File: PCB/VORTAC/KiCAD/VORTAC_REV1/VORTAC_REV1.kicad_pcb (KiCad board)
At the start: 4 copper layers, 68.4 x 24.7 mm, 13 parts, among them IC1 TMC2209-LA, J14 918-418K2023S40001, J15 STEPPER, J16 IO, J2 Molex Micro Fit 3.0, U2 STM32F103C8Tx, U6 SN65HVD232DR

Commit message: hallo
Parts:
- removed D7: NeoPixel_THT, LED_SMD:LED_Cree-PLCC4_2x2mm_CW
- removed J16: IO, Connector_JST:JST_PH_B5B-PH-K_1x05_P2.00mm_Vertical
- removed J2: Molex Micro Fit 3.0, Connector_JST:JST_PH_B6B-PH-K_1x06_P2.00mm_Vertical
- added C11: 0.1uF 50V, Capacitor_SMD:C_0603_1608Metric, F.Cu at (99.2, 69.1)
- added C12: 3.3nF, Capacitor_SMD:C_0603_1608Metric, F.Cu at (99.2, 71.6)
- added C14: 56pF, Capacitor_SMD:C_0603_1608Metric, F.Cu at (99.2, 74.2)
- added C16: 47uF, Capacitor_SMD:C_0805_2012Metric, F.Cu at (103.4, 76.8)
- added C18: 47uF, Capacitor_SMD:C_0805_2012Metric, F.Cu at (103.4, 79.9)
- added C20: 47uF, Capacitor_SMD:C_0805_2012Metric, F.Cu at (103.4, 82.9)
- added C21: 0.1uF 50V, Capacitor_SMD:C_0603_1608Metric, F.Cu at (127.1, 61.6)
- added C22: 0.1uF 50V, Capacitor_SMD:C_0603_1608Metric, F.Cu at (127.1, 64.1)
- added C23: 22nF X7R 10% 50V, Capacitor_SMD:C_0603_1608Metric, F.Cu at (127.1, 66.6)
- added C24: 0.1uF 50V, Capacitor_SMD:C_0603_1608Metric, F.Cu at (127.1, 69.1)
- added C26: 0.1uF 50V, Capacitor_SMD:C_0603_1608Metric, F.Cu at (127.1, 71.6)
- added C29: 0.1uF 50V, Capacitor_SMD:C_0603_1608Metric, F.Cu at (127.1, 74.2)
- added C3: 1uF, Capacitor_SMD:C_0603_1608Metric, F.Cu at (99.2, 61.6)
- added C33: 0.1uF 16V, Capacitor_SMD:C_0402_1005Metric, F.Cu at (120.8, 61.3)
- added C35: 0.1uF 16V, Capacitor_SMD:C_0402_1005Metric, F.Cu at (120.8, 63.3)
- added C36: 0.1uF 16V, Capacitor_SMD:C_0402_1005Metric, F.Cu at (120.8, 65.3)
- added C37: 0.1uF 16V, Capacitor_SMD:C_0402_1005Metric, F.Cu at (120.8, 67.2)
- added C38: 0.1uF 16V, Capacitor_SMD:C_0402_1005Metric, F.Cu at (120.8, 69.2)
- added C39: 0.1uF 16V, Capacitor_SMD:C_0402_1005Metric, F.Cu at (120.8, 71.2)
- added C40: 4.7uF 10V, Capacitor_SMD:C_0402_1005Metric, F.Cu at (123.7, 61.3)
- added C42: C_Small, Capacitor_SMD:C_0402_1005Metric, F.Cu at (123.7, 63.3)
- added C43: C_Small, Capacitor_SMD:C_0402_1005Metric, F.Cu at (123.7, 65.3)
- added C44: 10nF, Capacitor_SMD:C_0402_1005Metric, F.Cu at (123.7, 67.2)
- added C45: 1uF, Capacitor_SMD:C_0402_1005Metric, F.Cu at (123.7, 69.2)
- added C49: 0.1uF 16V, Capacitor_SMD:C_0402_1005Metric, F.Cu at (112.7, 81.0)
- added C5: 10uF 50V, Capacitor_SMD:C_1206_3216Metric, F.Cu at (108.5, 77.0)
- added C7: 0.1uF 50V, Capacitor_SMD:C_0603_1608Metric, F.Cu at (99.2, 64.1)
- added C8: 1uF, Capacitor_SMD:C_0603_1608Metric, F.Cu at (99.2, 66.6)
- added D5: D_Schottky, Diode_SMD:D_SOD-123, F.Cu at (127.0, 85.8)
- added D6: LED_Small, LED_SMD:LED_0402_1005Metric, F.Cu at (130.8, 61.3)
- added J1: DEBUG, ToolChanger:PinHeader_2x03_P1.27mm_Vertical, F.Cu at (146.7, 130.1)
- added J3: Conn_01x05, Connector_PinHeader_2.54mm:PinHeader_1x05_P2.54mm_Vertical, F.Cu at (174.2, 119.4)
- added L3: 10uH 15mA, Inductor_SMD:L_0805_2012Metric, F.Cu at (121.7, 73.5)
- added R1: 1K, Resistor_SMD:R_0603_1608Metric, F.Cu at (115.7, 88.5)
- added R2: 2K, Resistor_SMD:R_0603_1608Metric, F.Cu at (115.7, 90.5)
- added R23: 10k, Resistor_SMD:R_0402_1005Metric, F.Cu at (110.5, 88.0)
- added R25: 95k, Resistor_SMD:R_0402_1005Metric, F.Cu at (110.5, 90.0)
- added R28: 100k, Resistor_SMD:R_0402_1005Metric, F.Cu at (110.5, 92.0)
- added R29: 19.1k, Resistor_SMD:R_0402_1005Metric, F.Cu at (110.5, 94.0)
- added R3: 5.12K, Resistor_SMD:R_0402_1005Metric, F.Cu at (125.5, 88.5)
- added R31: 1K, Resistor_SMD:R_0402_1005Metric, F.Cu at (130.6, 63.3)
- added R32: 22K, Resistor_SMD:R_0402_1005Metric, F.Cu at (130.6, 65.3)
- added R33: 22K, Resistor_SMD:R_0402_1005Metric, F.Cu at (130.6, 67.3)
- added R35: 22R, Resistor_SMD:R_0402_1005Metric, F.Cu at (130.6, 69.3)
- added R36: 22R, Resistor_SMD:R_0402_1005Metric, F.Cu at (130.6, 71.3)
- added R37: R_Small, Resistor_SMD:R_0402_1005Metric, F.Cu at (130.6, 73.3)
- added R38: R_Small, Resistor_SMD:R_0402_1005Metric, F.Cu at (130.6, 75.3)
- added R4: 5.12K, Resistor_SMD:R_0402_1005Metric, F.Cu at (125.5, 90.5)
- added R5: 180, Resistor_SMD:R_0603_1608Metric, F.Cu at (115.7, 93.0)
- added R51: 1K, Resistor_SMD:R_0402_1005Metric, F.Cu at (110.5, 96.0)
- added R52: 10K, Resistor_SMD:R_0402_1005Metric, F.Cu at (110.5, 98.0)
- added R6: 180, Resistor_SMD:R_0603_1608Metric, F.Cu at (115.7, 95.5)
- added R7: 1K, Resistor_SMD:R_0603_1608Metric, F.Cu at (115.7, 98.0)
- added R8: 2K, Resistor_SMD:R_0603_1608Metric, F.Cu at (115.7, 100.5)
- added S1: ~, ToolChanger:OPB666N, F.Cu at (150.0, 119.0)
- added S2: ~, ToolChanger:OPB666N, F.Cu at (173.1, 108.5)
- added U1: TLV73333PDBV, Package_TO_SOT_SMD:SOT-23-5, F.Cu at (113.8, 77.7)
- added U3: STM32L011D_3-4_Px, Package_SO:TSSOP-14_4.4x5mm_P0.65mm, F.Cu at (164.0, 101.5)
- added U4: TPS54335ADRCR, ToolChanger:VSON-10-1EP_3x3mm_P0.5mm_EP1.65x2.4mm_ThermalVias, B.Cu at (157.5, 106.5)
- added U5: STM32G0B1C_B-C-E_Tx, Package_QFP:LQFP-48_7x7mm_P0.5mm, B.Cu at (174.5, 79.5)
- IC1: footprint ToolChanger:tmc_2209_ThermalPad -> ToolChanger:tmc_2209_package; moved to F.Cu
- J14: footprint ToolChanger:USB_C_Receptacle_XKB_U262-16XN-4BVC11 -> Connector_USB:USB_C_Receptacle_GCT_USB4115-03-C
- J15: footprint ToolChanger:JST_PH_S4B-PH-K_1x04_P2.00mm_Horizontal -> Connector_JST:JST_PH_B4B-PH-K_1x04_P2.00mm_Vertical; moved to B.Cu
- U6: moved to B.Cu
- moved J14 48.1 mm to (186.3, 101.6), turned to 135 degrees
- moved J15 33.2 mm to (160.5, 120.0), turned to 0 degrees
- moved IC1 23.8 mm to (150.0, 111.5), turned to -90 degrees
- moved C34 12.6 mm to (166.0, 112.5), turned to 0 degrees
- moved HSE1 11.8 mm to (172.9, 115.7)
- moved U2 11.1 mm to (165.8, 109.8)
- moved L2 8.56 mm to (157.0, 111.5)
- moved R30 5.26 mm to (126.5, 118.0), turned to 180 degrees
- moved U6 2.48 mm to (164.0, 101.6), turned to 180 degrees
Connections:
- U2 pad 10: HOST_USB_GATE -> unconnected-(U2-PA0-Pad10)
- U2 pad 11: LED_1_GATE -> unconnected-(U2-PA1-Pad11)
- U2 pad 13: ADXL_INT1 -> unconnected-(U2-PA3-Pad13)
- U2 pad 14: ADXL_CS -> unconnected-(U2-PA4-Pad14)
- U2 pad 15: ADXL_SCL -> unconnected-(U2-PA5-Pad15)
- U2 pad 16: ADXL_SDO -> unconnected-(U2-PA6-Pad16)
- U2 pad 17: ADXL_SDI -> unconnected-(U2-PA7-Pad17)
- U2 pad 21: THERM_1_PIN -> unconnected-(U2-PB10-Pad21)
- U2 pad 22: IO_3_OUT_PIN -> unconnected-(U2-PB11-Pad22)
- U2 pad 25: IO_2_OUT_PIN -> unconnected-(U2-PB12-Pad25)
- U2 pad 26: IO_1_OUT_PIN -> unconnected-(U2-PB13-Pad26)
- U2 pad 27: HEATER_GATE -> unconnected-(U2-PB14-Pad27)
- U2 pad 42: FAN_1_GATE -> unconnected-(U2-PB6-Pad42)
- U2 pad 43: FAN_2_GATE -> unconnected-(U2-PB7-Pad43)

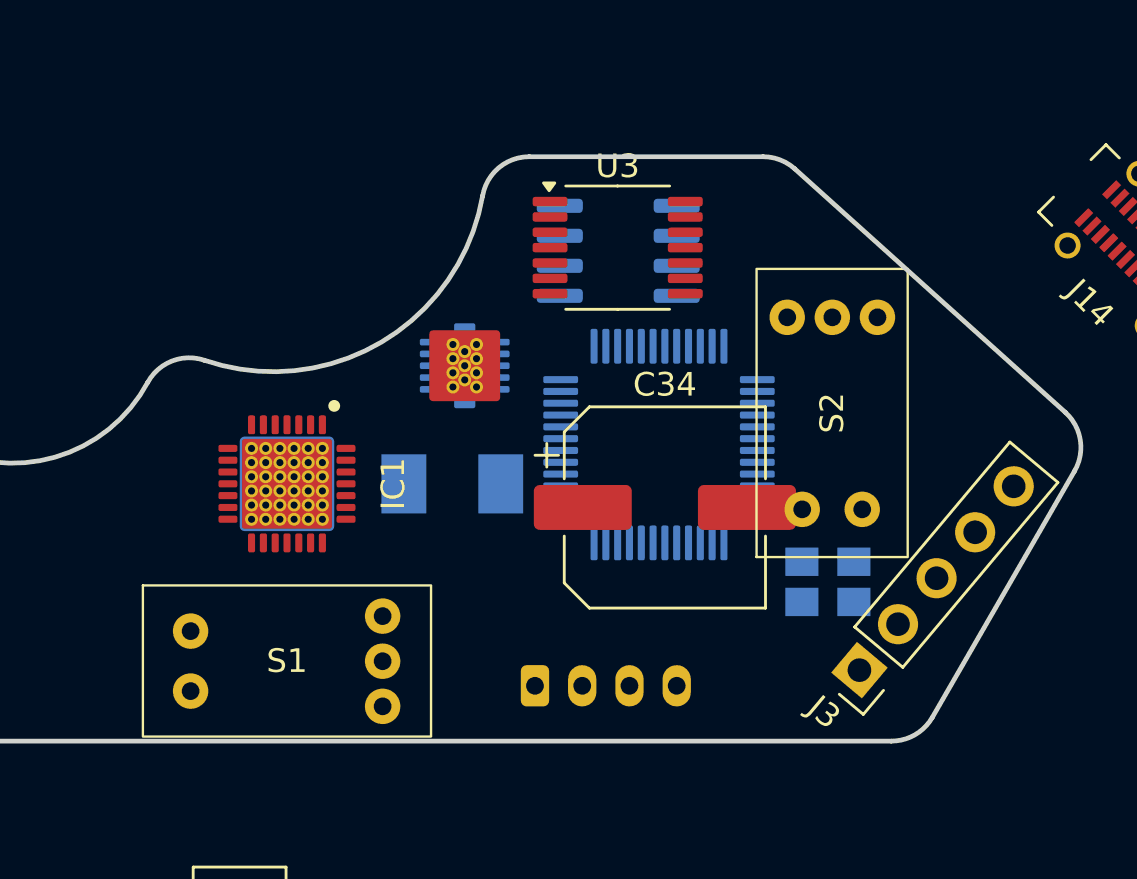
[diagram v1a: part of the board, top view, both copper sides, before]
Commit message: Added New EE_SX3350
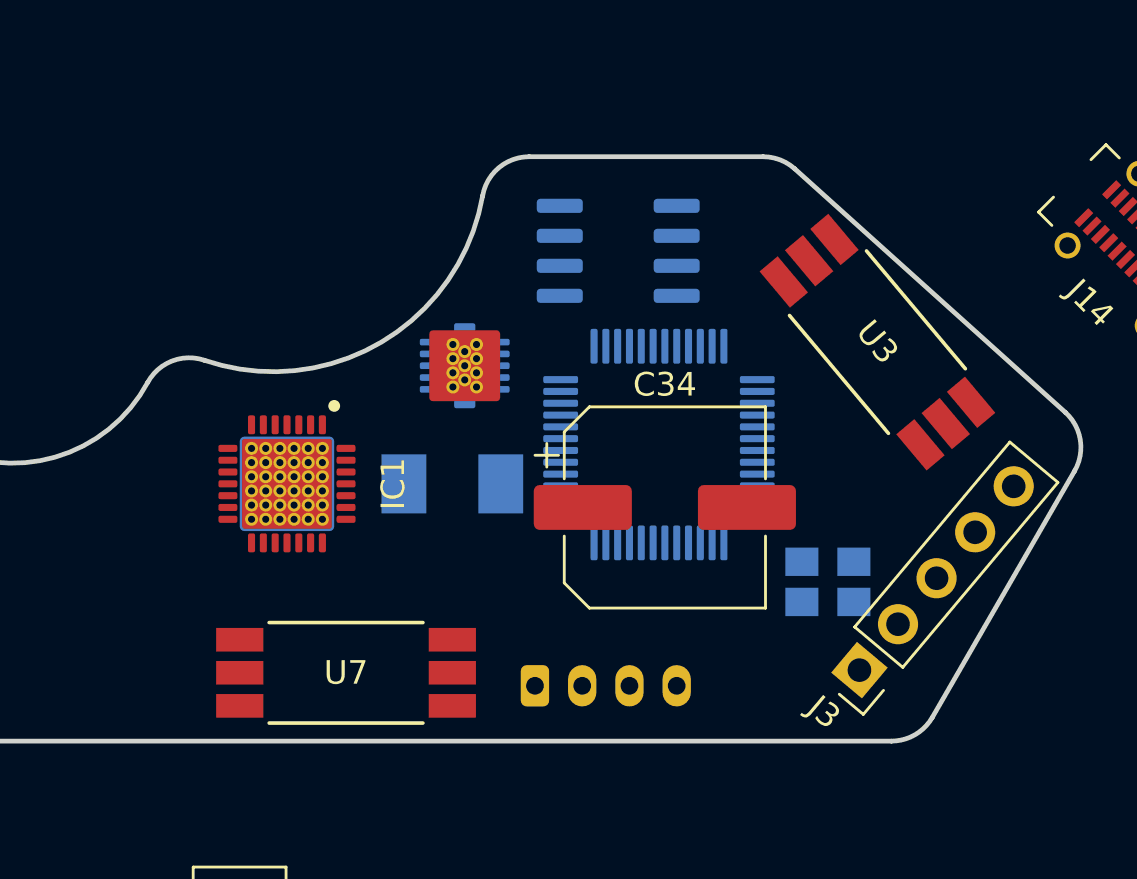
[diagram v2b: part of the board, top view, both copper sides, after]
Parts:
- removed S1, S2: ~, ToolChanger:OPB666N
- added U7: EE-SX3350, ToolChanger:SENSOR_EE-SX3350_OMR, F.Cu at (152.5, 119.5)
- U3: value STM32L011D_3-4_Px -> EE-SX3350; footprint Package_SO:TSSOP-14_4.4x5mm_P0.65mm -> ToolChanger:SENSOR_EE-SX3350_OMR
- moved U3 11.7 mm to (175.0, 105.5), turned to -50 degrees
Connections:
- R1 pad 1: Net-(S1-Out) -> Net-(U3-GND)
- R6 pad 2: Net-(S1-CA) -> Net-(U3-ANODE)
- U3 pad 1: unconnected-(U3-PB9-Pad1) -> Net-(U3-ANODE)
- U3 pad 2: unconnected-(U3-PC14-Pad2) -> GND
- U3 pad 3: unconnected-(U3-PC15-Pad3) -> GND
- U3 pad 4: unconnected-(U3-NRST-Pad4) -> GND
- U3 pad 5: unconnected-(U3-PA0-Pad5) -> +5V
- U3 pad 6: unconnected-(U3-PA1-Pad6) -> Net-(U3-GND)

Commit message: yipppieee
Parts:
- removed R31: 1K, Resistor_SMD:R_0402_1005Metric
- removed U5: STM32G0B1C_B-C-E_Tx, Package_QFP:LQFP-48_7x7mm_P0.5mm
- added C1: 470pF 100V, Capacitor_SMD:C_0603_1608Metric, F.Cu at (139.5, 110.4)
- added C10: 0.1uF 50V, Capacitor_SMD:C_0603_1608Metric, F.Cu at (139.5, 123.0)
- added C2: 0.1uF 50V, Capacitor_SMD:C_0603_1608Metric, F.Cu at (139.5, 112.9)
- added C4: 470pF 100V, Capacitor_SMD:C_0603_1608Metric, F.Cu at (139.5, 115.5)
- added C6: 470pF 100V, Capacitor_SMD:C_0603_1608Metric, F.Cu at (139.5, 118.0)
- added C9: 470pF 100V, Capacitor_SMD:C_0603_1608Metric, F.Cu at (139.5, 120.5)
- added JP1: Jumper, Connector_PinHeader_1.27mm:PinHeader_2x01_P1.27mm_Vertical, F.Cu at (143.7, 110.8)
- added L1: Common Choke, Inductor_SMD:L_CommonModeChoke_Coilcraft_0805USB, F.Cu at (143.0, 114.5)
- added R10: 120R, Resistor_SMD:R_0402_1005Metric, F.Cu at (143.0, 119.5)
- added R9: 100R, Resistor_SMD:R_0402_1005Metric, F.Cu at (143.0, 117.5)
- C22: value 0.1uF 50V -> 4.7uF 50V
- C34: footprint Capacitor_SMD:CP_Elec_8x6.9 -> Capacitor_SMD:CP_Elec_6.3x7.7
- J14: moved to B.Cu
- R30, R34: value 0.1R 1% -> 0.22R 1%
- R32, R33: value 22K -> 10K
- moved J1 33.0 mm to (170.3, 107.0), turned to 180 degrees
- moved U2 21.8 mm to (186.8, 104.2)
- moved J14 13.5 mm to (174.2, 95.3), turned to 0 degrees
- moved J3 10.9 mm to (181.0, 110.8), turned to -30 degrees
- moved U3 3.16 mm to (174.0, 108.5), turned to 90 degrees
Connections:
- IC1 pad 14: TMC_UART_RX -> TMC_UART
- R1 pad 1: Net-(U3-GND) -> Net-(U3-OUTPUT)
- R33 pad 1: TMC_UART_RX -> TMC_UART
- R33 pad 2: GND -> +3V3
- R7 pad 1: Net-(U7-GND) -> Net-(U7-OUTPUT)
- U2 pad 10: unconnected-(U2-PA0-Pad10) -> ENDSTOP_Z
- U2 pad 11: unconnected-(U2-PA1-Pad11) -> ENDSTOP_X
- U2 pad 30: TMC_UART_TX -> TMC_UART
- U2 pad 31: TMC_UART_RX -> unconnected-(U2-PA10-Pad31)
- U2 pad 38: TMC_DIAG -> Net-(U2-PA15)
- U3 pad 4: GND -> +5V
- U3 pad 5: +5V -> Net-(U3-OUTPUT)
- U3 pad 6: Net-(U3-GND) -> GND
- U6 pad 6: CAN_L -> Net-(U6-CANL)
- U6 pad 7: CAN_H -> Net-(U6-CANH)
- U7 pad 4: GND -> +5V
- U7 pad 5: +5V -> Net-(U7-OUTPUT)
- U7 pad 6: Net-(U7-GND) -> GND

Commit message: Fixed Library stuff
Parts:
- added C13: 0.1uF 50V, Capacitor_SMD:C_0603_1608Metric, F.Cu at (173.8, 101.8)
- added R11: 10K, Resistor_SMD:R_0402_1005Metric, F.Cu at (177.7, 110.6)
- added R12: 10K, Resistor_SMD:R_0402_1005Metric, F.Cu at (174.7, 115.4)
- added SW1: Boot, Vortac:KEY-SMD_B3U-1000PM, B.Cu at (162.5, 100.0)
- added SW2: Reset, Vortac:KEY-SMD_B3U-1000PM, B.Cu at (165.8, 100.0)
- C10, C21, C22, C23, C24, C26, C5, C6, C9, D5, JP1, R1, R10, R2, R35, R36, R37, R38, R5, R6, R7, R8, R9: moved to B.Cu
- IC1: footprint ToolChanger:tmc_2209_package -> Vortac:tmc_2209_package
- J1: footprint ToolChanger:PinHeader_2x03_P1.27mm_Vertical -> Vortac:PinHeader_2x03_P1.27mm_Vertical; moved to B.Cu
- J14: footprint Connector_USB:USB_C_Receptacle_GCT_USB4115-03-C -> Vortac:USB-C-TH_HANBO_MC-118LD-H65
- L1: footprint Inductor_SMD:L_CommonModeChoke_Coilcraft_0805USB -> Vortac:L_CommonModeChoke_Coilcraft_0805USB
- L2: footprint ToolChanger:L_Sunlord_MWSA0518_5.4x5.2mm -> Vortac:L_Sunlord_MWSA0518_5.4x5.2mm
- R30, R34, U6: moved to F.Cu
- U2: value STM32F103C8Tx -> STM32F103C8T6
- U3, U7: footprint ToolChanger:SENSOR_EE-SX3350_OMR -> Vortac:SENSOR_EE-SX3350_OMR
- U4: footprint ToolChanger:VSON-10-1EP_3x3mm_P0.5mm_EP1.65x2.4mm_ThermalVias -> Vortac:VSON-10-1EP_3x3mm_P0.5mm_EP1.65x2.4mm_ThermalVias
- moved C11 86.1 mm to (168.8, 119.8)
- moved C12 85.6 mm to (168.8, 121.4)
- moved C18 77.4 mm to (171.8, 116.0)
- moved C20 76.9 mm to (171.8, 118.0)
- moved C14 74.7 mm to (160.0, 117.4)
- moved C3 73.7 mm to (148.6, 116.2)
- moved C7 73.6 mm to (151.6, 115.8)
- moved C5 72.8 mm to (174.5, 107.8), turned to 180 degrees
- moved C8 70.8 mm to (151.6, 114.2)
- moved C21 70.2 mm to (179.6, 108.3), turned to -90 degrees
- moved C40 69.9 mm to (177.7, 105.7)
- moved C22 69.8 mm to (176.7, 113.2), turned to -90 degrees
- moved L3 69.6 mm to (172.1, 121.4)
- moved C42 69.3 mm to (177.7, 106.7)
- moved C43 68.7 mm to (177.7, 107.7)
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
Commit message: pls merge Jenno
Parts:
- added U5: AS5047D, Package_SO:TSSOP-14_4.4x5mm_P0.65mm, F.Cu at (140.1, 116.5)

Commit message: Kanoolaaaa
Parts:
- removed U6: SN65HVD232DR, Package_SO:SOIC-8_3.9x4.9mm_P1.27mm
- added C15: 0.1uF 50V, Capacitor_SMD:C_0603_1608Metric, B.Cu at (142.7, 111.5)
- added U8: TJA1044GTK/3Z, Vortac:HVSON-8-1EP_3x3mm_P0.65mm_EP1.6x2.4mm, F.Cu at (131.9, 117.2)
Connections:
- C35 pad 1: +3V3 -> unconnected-(C35-Pad1)
- U5 pad 1: unconnected-(U5-~{CS}-Pad1) -> AS_CS
- U5 pad 11: unconnected-(U5-VDD-Pad11) -> +3V3
- U5 pad 12: unconnected-(U5-VDD3V3-Pad12) -> +3V3
- U5 pad 13: unconnected-(U5-GND-Pad13) -> GND
- U5 pad 2: unconnected-(U5-CLK-Pad2) -> AS_CLK
- U5 pad 3: unconnected-(U5-MISO-Pad3) -> AS_MISO
- U5 pad 4: unconnected-(U5-MOSI-Pad4) -> AS_MOSI
- U5 pad 5: unconnected-(U5-TST-Pad5) -> GND

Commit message: Liebe Griasse zurrueck
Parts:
- removed R37: R_Small, Resistor_SMD:R_0402_1005Metric
- added C17: 0.1uF 16V, Capacitor_SMD:C_0402_1005Metric, F.Cu at (179.5, 102.5)
- C42, C43: value C_Small -> 16pF
- J14: footprint Vortac:USB-C-TH_HANBO_MC-118LD-H65 -> Vortac:USB-C-SMD_TYPEC-303-ACP16
- R38: value R_Small -> 22R
- moved U2 24.8 mm to (190.2, 112.7)
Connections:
- C35 pad 1: unconnected-(C35-Pad1) -> +3V3
- C42 pad 2: GND1 -> GND
- C43 pad 1: Net-(C43-Pad1) -> HSE_OSC_OUT
- C43 pad 2: GND1 -> GND
- HSE1 pad 2: GND1 -> GND
- HSE1 pad 3: Net-(C43-Pad1) -> HSE_OSC_OUT
- HSE1 pad 4: GND1 -> GND
- J1 pad 4: GND -> DEBUG_SWO
- U2 pad 14: unconnected-(U2-PA4-Pad14) -> AS_NCS
- U2 pad 15: unconnected-(U2-PA5-Pad15) -> AS_CLK
- U2 pad 16: unconnected-(U2-PA6-Pad16) -> AS_MOSI
- U2 pad 17: unconnected-(U2-PA7-Pad17) -> AS_MISO
- U2 pad 39: unconnected-(U2-PB3-Pad39) -> DEBUG_SWO
- U2 pad 9: +3.3VA -> +3V3
- U5 pad 1: AS_CS -> AS_NCS

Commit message: Gschenkle
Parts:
- C10, C15, C21, C22, C23, C24, C26, C6, C9, HSE1, J15, JP1, L2, R1, R10, R35, R36, R38, R7, U4: moved to F.Cu
- D5: footprint Diode_SMD:D_SOD-123 -> Diode_SMD:D_SOD-323; moved to F.Cu
- IC1, R33, R52: moved to B.Cu
- R2, R8: value 2K -> 10K; footprint Resistor_SMD:R_0603_1608Metric -> Resistor_SMD:R_0402_1005Metric; moved to F.Cu
- R5, R6: value 180 -> 330R; moved to F.Cu
- U3, U7: value EE-SX3350 -> EE-SX4350
- moved C10 82.3 mm to (137.9, 40.0), turned to 0 degrees
- moved C29 80.5 mm to (141.9, 45.1)
- moved C24 79.7 mm to (141.9, 40.0), turned to 0 degrees
- moved C6 76.9 mm to (133.8, 47.6), turned to 0 degrees
- moved C26 76.8 mm to (141.9, 42.6), turned to 0 degrees
- moved C22 76.3 mm to (137.9, 47.6), turned to 0 degrees
- moved C21 75.8 mm to (137.9, 45.1), turned to 0 degrees
- moved C9 73.7 mm to (133.8, 50.1), turned to 0 degrees
- moved C23 73.3 mm to (137.9, 50.1), turned to 0 degrees
- moved C4 72.8 mm to (133.8, 45.1), turned to 0 degrees
- moved C2 70.5 mm to (133.8, 42.6), turned to 0 degrees
- moved C1 69.8 mm to (133.8, 40.0), turned to 0 degrees
- moved C13 69.2 mm to (137.9, 42.6)
- moved C37 67.0 mm to (148.2, 48.3)
- moved C38 66.1 mm to (148.2, 50.2)
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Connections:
- R2 pad 1: ENDSTOP_Z -> +3V3
- R2 pad 2: GND -> ENDSTOP_Z
- R5 pad 1: +3V3 -> +5V
- R6 pad 1: +3V3 -> +5V
- R8 pad 1: ENDSTOP_X -> +3V3
- R8 pad 2: GND -> ENDSTOP_X
- R9 pad 2: TMC_DIAG -> unconnected-(R9-Pad2)
- U2 pad 10: ENDSTOP_Z -> TMC_ENN
- U2 pad 11: ENDSTOP_X -> TMC_DIR
- U2 pad 12: unconnected-(U2-PA2-Pad12) -> TMC_UART
- U2 pad 13: unconnected-(U2-PA3-Pad13) -> TMC_STEP
- U2 pad 14: AS_NCS -> unconnected-(U2-PA4-Pad14)
- U2 pad 15: AS_CLK -> unconnected-(U2-PA5-Pad15)
- U2 pad 16: AS_MOSI -> unconnected-(U2-PA6-Pad16)
- U2 pad 17: AS_MISO -> unconnected-(U2-PA7-Pad17)
- U2 pad 18: unconnected-(U2-PB0-Pad18) -> TMC_DIAG
- U2 pad 25: unconnected-(U2-PB12-Pad25) -> AS_NSS
- U2 pad 26: unconnected-(U2-PB13-Pad26) -> AS_SCK
- U2 pad 27: unconnected-(U2-PB14-Pad27) -> AS_MISO
- U2 pad 28: TMC_STEP -> AS_MOSI
- U2 pad 29: TMC_DIR -> unconnected-(U2-PA8-Pad29)
- U2 pad 30: TMC_UART -> unconnected-(U2-PA9-Pad30)
- U2 pad 40: TMC_ENN -> unconnected-(U2-PB4-Pad40)
- U2 pad 41: TOOL_ID_PIN -> unconnected-(U2-PB5-Pad41)
- U5 pad 1: AS_NCS -> AS_NSS
- U5 pad 2: AS_CLK -> AS_SCK
